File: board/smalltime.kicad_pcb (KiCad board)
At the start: 2 copper layers, 80 x 56 mm, 45 parts, among them IC1 STM32F030K6T6, IC2 DS3231MZ, IC3 ADP3338, J1 MICROUSB, P1 SWD, P2 SWD_TC, Q1 TEPT4400, Q2 Q_NMOS_GDS, Q3 Q_NMOS_GDS, Q4 Q_NMOS_GDS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

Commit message: Flipped and routed 7segs
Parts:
- moved BT1 75.2 mm to (146.2, 49.8), turned to 180 degrees
- moved IC2 71.6 mm to (130.0, 48.8), turned to 90 degrees
- moved R1 66.4 mm to (126.2, 46.5), turned to 90 degrees
- moved R2 64.3 mm to (124.8, 46.5), turned to 90 degrees
- moved C6 63.3 mm to (128.8, 53.8), turned to 180 degrees
- moved C7 26.7 mm to (146.2, 80.5), turned to 180 degrees
- moved C8 22.2 mm to (143.0, 80.5)
- moved IC3 21.9 mm to (144.5, 78.1)
- moved SW2 9.30 mm to (77.5, 53.0)
- moved SW1 9.25 mm to (77.5, 43.2)
- moved P1 8.50 mm to (78.6, 80.3)
- moved P2 8.50 mm to (78.4, 71.2)
- turned U1 to 180 degrees
- turned U2 to 180 degrees
- turned U3 to 180 degrees
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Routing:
- net /SEG_DP: track 0.00 -> 175.8 mm, vias 0 -> 7
- net /SEG_C: track 0.00 -> 170.1 mm, vias 0 -> 7
- net /SEG_D: track 0.00 -> 160.7 mm, vias 0 -> 7
- net /SEG_E: track 0.00 -> 146.1 mm
- net /SEG_A: track 0.00 -> 141.9 mm, vias 0 -> 6
- net /SEG_F: track 0.00 -> 141.3 mm, vias 0 -> 6
- net /SEG_G: track 0.63 -> 135.9 mm, vias 0 -> 3
- net /SEG_B: track 0.00 -> 134.9 mm, vias 0 -> 3
- net Net-(BT1-Pad1): track 0.00 -> 7.93 mm
- net Net-(Q6-Pad3): track 0.20 -> 3.48 mm
- net +3V3: track 0.00 -> 2.38 mm
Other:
- net class Default: via_dia 0.6 -> 0.8

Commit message: Did some more routing.
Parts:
- moved R3 82.6 mm to (114.9, 40.0)
- moved Q1 82.6 mm to (113.7, 36.8)
- moved R11 68.8 mm to (88.4, 69.1), turned to 270 degrees
- moved R7 67.6 mm to (91.4, 69.1), turned to 270 degrees
- moved C2 62.7 mm to (99.6, 75.8), turned to 270 degrees
- moved R10 62.1 mm to (93.2, 83.3), turned to 90 degrees
- moved R8 61.9 mm to (92.9, 69.1), turned to 270 degrees
- moved R6 61.8 mm to (89.9, 69.1), turned to 270 degrees
- moved R9 61.4 mm to (91.7, 83.3), turned to 90 degrees
- moved C1 60.9 mm to (98.1, 75.8), turned to 270 degrees
- moved C3 60.5 mm to (97.9, 79.7), turned to 270 degrees
- moved C5 59.6 mm to (96.4, 79.7), turned to 270 degrees
- moved R4 55.5 mm to (90.2, 83.3), turned to 90 degrees
- moved R5 51.2 mm to (88.7, 83.3), turned to 90 degrees
- moved C4 50.1 mm to (84.3, 70.8), turned to 90 degrees
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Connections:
- IC1 pad 10: (no net) -> Net-(IC1-Pad10)
- IC1 pad 11: (no net) -> Net-(IC1-Pad11)
- IC1 pad 12: (no net) -> Net-(IC1-Pad12)
- IC1 pad 13: (no net) -> Net-(IC1-Pad13)
- IC1 pad 14: (no net) -> Net-(IC1-Pad14)
- IC1 pad 15: (no net) -> Net-(IC1-Pad15)
- IC1 pad 18: (no net) -> Net-(IC1-Pad18)
- IC1 pad 19: (no net) -> Net-(IC1-Pad19)
- IC1 pad 2: (no net) -> Net-(IC1-Pad2)
- IC1 pad 20: (no net) -> Net-(IC1-Pad20)
- IC1 pad 21: (no net) -> Net-(IC1-Pad21)
- IC1 pad 22: (no net) -> Net-(IC1-Pad22)
- IC1 pad 25: (no net) -> /DIG1
- IC1 pad 26: (no net) -> Net-(IC1-Pad26)
- IC1 pad 27: (no net) -> Net-(IC1-Pad27)
- IC1 pad 28: (no net) -> Net-(IC1-Pad28)
- IC1 pad 29: (no net) -> Net-(IC1-Pad29)
- IC1 pad 3: (no net) -> Net-(IC1-Pad3)
- IC1 pad 30: (no net) -> /DIG2
- IC1 pad 6: (no net) -> Net-(IC1-Pad6)
- IC1 pad 7: (no net) -> Net-(IC1-Pad7)
- IC1 pad 8: (no net) -> Net-(IC1-Pad8)
- IC1 pad 9: (no net) -> Net-(IC1-Pad9)
- IC2 pad 1: (no net) -> Net-(IC2-Pad1)
- IC2 pad 3: (no net) -> Net-(IC2-Pad3)
- IC2 pad 4: (no net) -> Net-(IC2-Pad4)
- J1 pad 2: (no net) -> Net-(J1-Pad2)
- J1 pad 3: (no net) -> Net-(J1-Pad3)
- J1 pad 4: (no net) -> Net-(J1-Pad4)
- J1 pad S: (no net) -> Net-(J1-PadS)
- P1 pad 6: (no net) -> Net-(P1-Pad6)
- P1 pad 7: (no net) -> Net-(P1-Pad7)
- P1 pad 8: (no net) -> Net-(P1-Pad8)
- P2 pad 6: (no net) -> Net-(P2-Pad6)
- Q1 pad 2: (no net) -> /LIGHT_EN
- Q2 pad 1: (no net) -> /DIG1
- Q3 pad 1: (no net) -> /DIG2
- Q4 pad 1: (no net) -> /DIG3
- Q5 pad 1: (no net) -> /DIG4
- Q6 pad 1: (no net) -> /DIG5
- Q7 pad 1: (no net) -> /DIG6
- Q8 pad 1: (no net) -> /DIG7
- Q9 pad 1: (no net) -> /DIG8
- R10 pad 2: (no net) -> Net-(IC1-Pad29)
- R11 pad 2: (no net) -> Net-(R11-Pad2)
- R4 pad 2: (no net) -> Net-(IC1-Pad27)
- R5 pad 2: (no net) -> Net-(IC1-Pad26)
- R6 pad 2: (no net) -> Net-(R6-Pad2)
- R7 pad 2: (no net) -> Net-(R7-Pad2)
- R8 pad 2: (no net) -> Net-(R8-Pad2)
- R9 pad 2: (no net) -> Net-(IC1-Pad28)
- SW1 pad 1: (no net) -> /SW_INC
- SW2 pad 1: (no net) -> /SW_SET
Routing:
- net +3V3: track 2.38 -> 158.5 mm, vias 0 -> 1
- net /SEG_B: track 134.9 -> 208.1 mm, vias 3 -> 5
- net /SEG_G: track 135.9 -> 198.9 mm, vias 3 -> 6
- net /SEG_A: track 141.9 -> 204.3 mm, vias 6 -> 8
- net /SEG_F: track 141.3 -> 199.7 mm, vias 6 -> 8
- net GND: track 0.00 -> 53.1 mm, vias 0 -> 29
- net Net-(Q2-Pad3): track 0.00 -> 35.3 mm, vias 0 -> 2
- net /~RST: track 0.00 -> 34.9 mm
- net Net-(Q8-Pad3): track 0.00 -> 25.8 mm
- net Net-(Q9-Pad3): track 0.00 -> 24.8 mm
- net Net-(Q5-Pad3): track 0.00 -> 24.6 mm, vias 0 -> 2
- net Net-(Q3-Pad3): track 0.00 -> 24.6 mm, vias 0 -> 2
- net Net-(Q4-Pad3): track 0.00 -> 24.5 mm, vias 0 -> 2
- net Net-(Q7-Pad3): track 0.00 -> 24.4 mm
- net Net-(Q6-Pad3): track 3.48 -> 24.7 mm
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- added copper zone on F.Cu, net +3V3
- added copper zone on B.Cu, net GND
- added copper zone on F.Cu, net GND

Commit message: Nominally finished routing
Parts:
- moved BT1 52.6 mm to (93.7, 48.5), turned to 0 degrees
- moved R2 44.4 mm to (100.8, 83.1), turned to 180 degrees
- moved R1 42.4 mm to (100.8, 81.6), turned to 180 degrees
- moved IC2 34.0 mm to (109.8, 76.1), turned to 180 degrees
- moved C6 27.4 mm to (114.8, 77.3), turned to 270 degrees
- moved R3 24.8 mm to (90.1, 39.3), turned to 180 degrees
- moved Q1 20.0 mm to (93.8, 39.0)
- moved R5 6.20 mm to (82.9, 81.1)
- moved R11 2.21 mm to (86.3, 68.4)
- moved R6 2.21 mm to (87.8, 68.4)
- moved R7 2.21 mm to (89.3, 68.4)
- moved R8 2.21 mm to (90.8, 68.4)
- moved R10 1.80 mm to (91.4, 83.4)
- moved R4 1.80 mm to (88.4, 83.4)
- moved R9 1.80 mm to (89.9, 83.4)
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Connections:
- IC1 pad 10: Net-(IC1-Pad10) -> /LIGHT_SENSE
- IC1 pad 11: Net-(IC1-Pad11) -> /DIG5
- IC1 pad 18: Net-(IC1-Pad18) -> /SW_INC
- IC1 pad 19: Net-(IC1-Pad19) -> /SW_SET
- IC1 pad 2: Net-(IC1-Pad2) -> /DIG3
- IC1 pad 20: Net-(IC1-Pad20) -> /DIG6
- IC1 pad 29: Net-(IC1-Pad29) -> /I2C_SCL
- IC1 pad 3: Net-(IC1-Pad3) -> /DIG4
- IC1 pad 30: /DIG2 -> /I2C_SDA
- IC1 pad 6: Net-(IC1-Pad6) -> /DIG2
- IC1 pad 7: Net-(IC1-Pad7) -> /DIG8
- IC1 pad 8: Net-(IC1-Pad8) -> /DIG7
- IC1 pad 9: Net-(IC1-Pad9) -> /LIGHT_EN
- R10 pad 2: Net-(IC1-Pad29) -> Net-(IC1-Pad28)
- R11 pad 2: Net-(R11-Pad2) -> Net-(IC1-Pad15)
- R4 pad 2: Net-(IC1-Pad27) -> Net-(IC1-Pad26)
- R5 pad 2: Net-(IC1-Pad26) -> Net-(IC1-Pad22)
- R6 pad 2: Net-(R6-Pad2) -> Net-(IC1-Pad14)
- R7 pad 2: Net-(R7-Pad2) -> Net-(IC1-Pad13)
- R8 pad 2: Net-(R8-Pad2) -> Net-(IC1-Pad12)
- R9 pad 2: Net-(IC1-Pad28) -> Net-(IC1-Pad27)
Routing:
- net /DIG8: track 0.00 -> 77.5 mm, vias 0 -> 2
- net /DIG4: track 0.00 -> 65.3 mm, vias 0 -> 4
- net /DIG7: track 0.00 -> 56.5 mm, vias 0 -> 2
- net /DIG6: track 0.00 -> 47.8 mm
- net /SW_INC: track 0.00 -> 41.5 mm
- net /DIG3: track 0.00 -> 39.2 mm, vias 0 -> 2
- net /SEG_D: track 160.7 -> 122.7 mm, vias 7 -> 4
- net /DIG5: track 0.00 -> 37.4 mm
- net /LIGHT_SENSE: track 3.38 -> 39.3 mm
- net /LIGHT_EN: track 0.00 -> 34.3 mm
- net /SW_SET: track 0.00 -> 32.4 mm
- net /SEG_E: track 148.7 -> 117.6 mm, vias 0 -> 2
- net Net-(BT1-Pad1): track 7.93 -> 36.2 mm, vias 0 -> 2
- net Net-(Q4-Pad3): track 24.5 -> 51.5 mm, vias 2 -> 0
- net Net-(Q3-Pad3): track 24.6 -> 47.0 mm, vias 2 -> 0
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
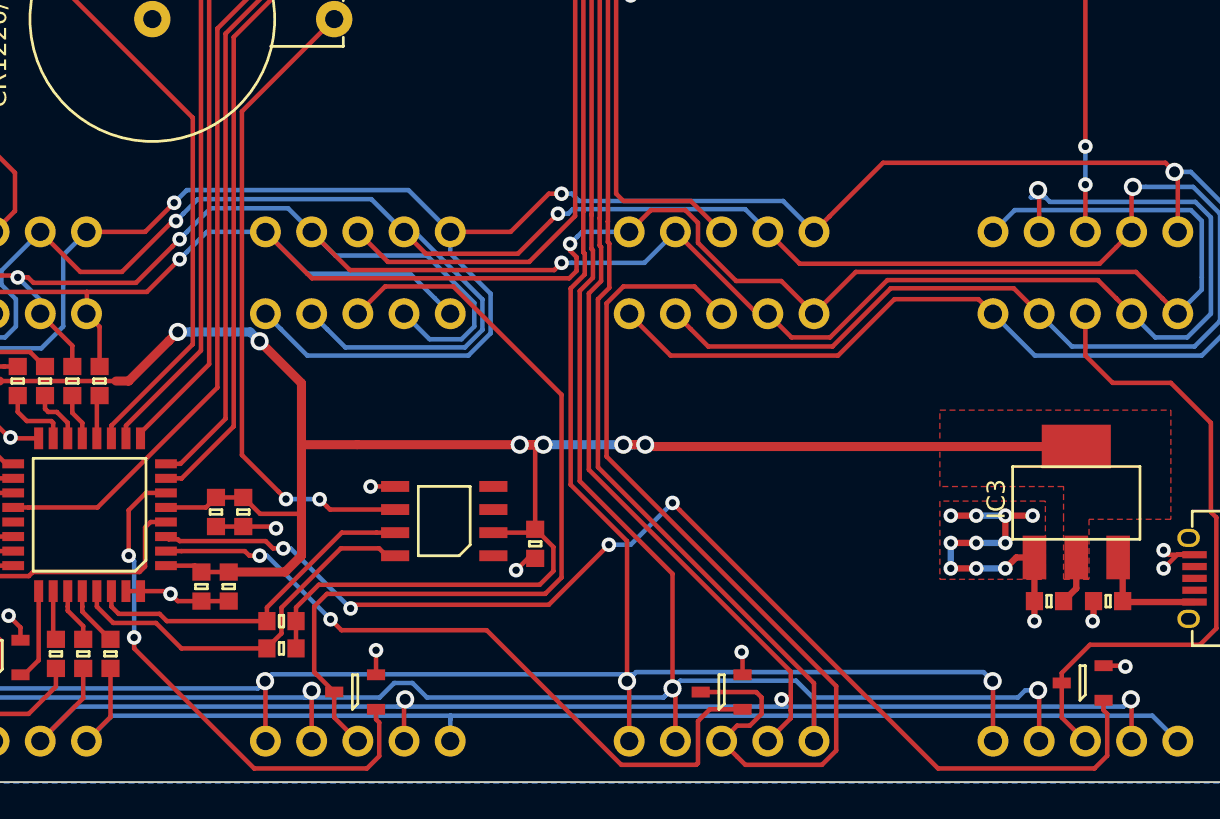
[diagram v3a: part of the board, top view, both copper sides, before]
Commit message: minor routing improvements
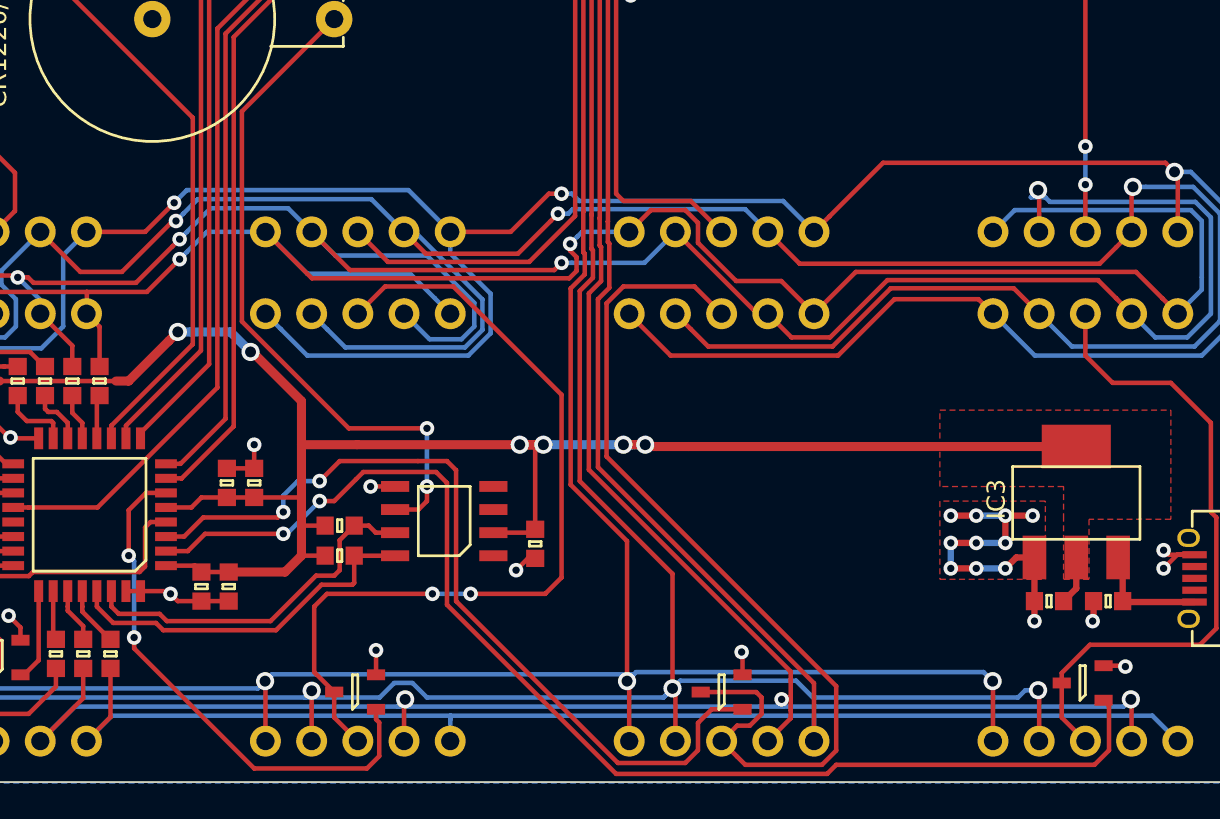
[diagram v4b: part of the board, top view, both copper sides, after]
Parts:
- moved R1 6.15 mm to (104.0, 76.3), turned to 0 degrees
- moved R2 6.02 mm to (104.0, 78.0), turned to 0 degrees
- moved C1 1.71 mm to (97.8, 74.0), turned to 90 degrees
- moved C2 1.71 mm to (99.3, 74.0), turned to 90 degrees
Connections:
- IC1 pad 2: /DIG3 -> /DIG4
- IC1 pad 3: /DIG4 -> /DIG3
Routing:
- net +3V3: track 152.3 -> 134.0 mm
- net /DIG3: track 39.2 -> 47.1 mm
- net /DIG4: track 65.3 -> 67.9 mm, vias 4 -> 2
- net Net-(BT1-Pad1): track 36.2 -> 37.8 mm
- net /I2C_SDA: track 19.2 -> 20.1 mm
- net /I2C_SCL: track 21.5 -> 20.8 mm
- net GND: track 66.7 -> 66.2 mm
- net Net-(Q3-Pad3): vias 0 -> 2

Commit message: Schematic checking/finishing
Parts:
- Q2, Q3, Q4, Q5, Q6, Q7, Q8, Q9: value Q_NMOS_GDS -> Q_NMOS_GSD
- R10, R11, R4, R5, R6, R7, R8, R9: value 300 -> 160

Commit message: Finishing touches and checking, silk
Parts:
- added TP1: SDA, smalltime:testpoint, F.Cu at (99.7, 80.4)
- added TP2: SCL, smalltime:testpoint, F.Cu at (99.3, 83.3)
- added TP3: GND, smalltime:testpoint, F.Cu at (96.7, 83.3)
- moved BT1 1.84 mm to (94.6, 50.1)
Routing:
- net GND: track 66.2 -> 80.4 mm, vias 29 -> 25
- net Net-(Q7-Pad3): track 44.9 -> 37.1 mm
- net +3V3: track 134.0 -> 140.7 mm
- net /SEG_D: track 122.7 -> 119.4 mm
- net Net-(BT1-Pad1): track 37.8 -> 36.4 mm
- net /I2C_SCL: track 20.8 -> 22.0 mm
- net /I2C_SDA: track 20.1 -> 21.3 mm
- net /SEG_A: track 208.9 -> 207.7 mm
- net /DIG3: track 47.1 -> 46.4 mm
- net Net-(Q5-Pad3): track 36.0 -> 36.7 mm
- net /SEG_C: track 150.4 -> 149.9 mm
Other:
- net class Default: clearance 0.2 -> 0.18
- rule trace_clearance: 0.2 -> 0.18
- board text added: "+"
- board text added: "DAVID TURNER 2017-08-01 REVISION 1"
